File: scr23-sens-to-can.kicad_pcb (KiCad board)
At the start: 2 copper layers, 78 x 62.5 mm, 65 parts, among them IC1 ADS1256IDBRG4, J3 Conn_ST_STDC14, J4 6437288-2, SW1 SW_SPDT, U1 SRV05-4, U2 SRV05-4, U3 LM4040DCK-2.5, U4 TJA1042T-3, U5 AP7370-33Y-13, U6 ADP7142AUJZ-5.0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

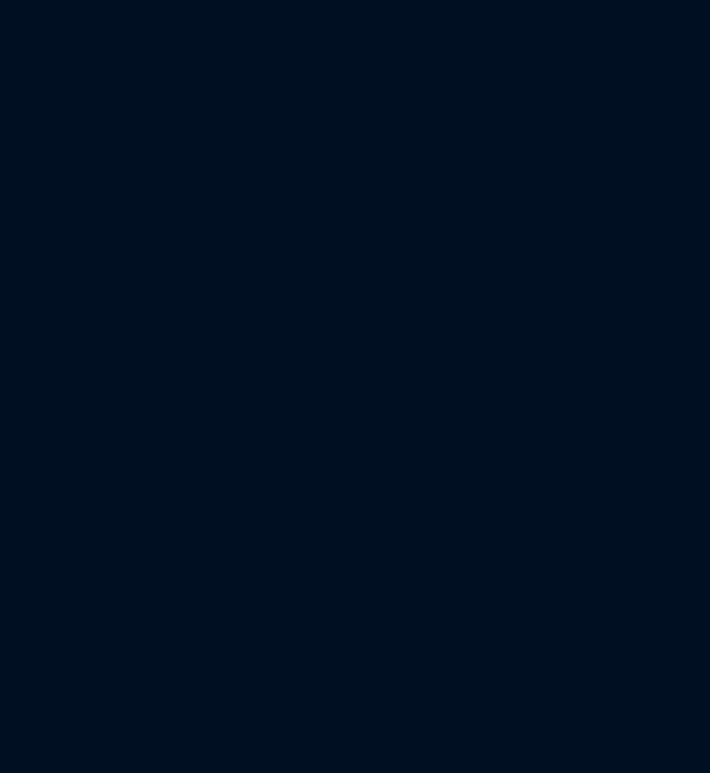
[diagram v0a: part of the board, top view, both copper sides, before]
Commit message: add uC crystal, finish swap to ads8168, need to add some footprints to passives and redo layout
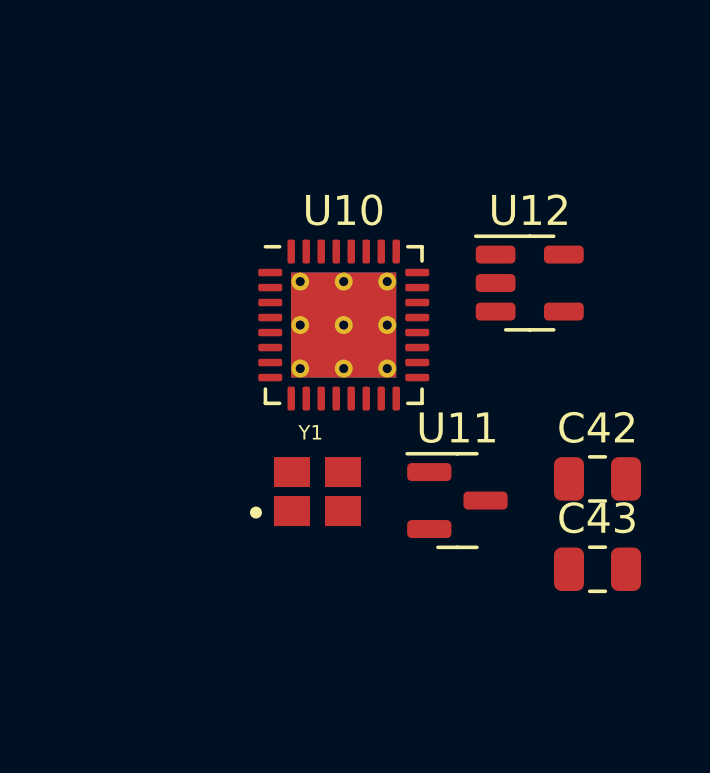
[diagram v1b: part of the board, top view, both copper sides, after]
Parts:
- added C42: 1uF, Capacitor_SMD:C_0805_2012Metric, F.Cu at (178.6, 102.7)
- added C43: 1uF, Capacitor_SMD:C_0805_2012Metric, F.Cu at (178.6, 105.7)
- added U10: ADS8168IRHBT, Package_DFN_QFN:VQFN-32-1EP_5x5mm_P0.5mm_EP3.5x3.5mm_ThermalVias, F.Cu at (170.2, 97.5)
- added U11: LM4040DBZ-5, Package_TO_SOT_SMD:SOT-23, F.Cu at (174.0, 103.4)
- added U12: OPA320AIDBVR, Package_TO_SOT_SMD:SOT-23-5, F.Cu at (176.4, 96.1)
- added Y1: ECS-160-8-36B-CKY-TR3, scr23-sens-to-can-main:XTAL_ECS-163.84-10-36-JGN-TR, F.Cu at (169.3, 103.1)
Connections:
- net /ADC_CS renamed ADC_CS
- U8 pad 11: /DATA_RDY -> DATA_READY
- U8 pad 13: /SPI1_SCK -> ADC_SCLK
- U8 pad 14: /SPI1_MISO -> ADC_SDO
- U8 pad 15: /SPI1_MOSI -> ADC_SDI
- U8 pad 3: Net-(U8A-PC14-OSC32_IN) -> unconnected-(U8A-PC14-OSC32_IN-Pad3)
- U8 pad 4: Net-(U8A-PC15-OSC32_OUT) -> unconnected-(U8A-PC15-OSC32_OUT-Pad4)
- U8 pad 5: Net-(U8A-PF0-OSC_IN) -> /OSC_IN
- U8 pad 6: Net-(U8A-PF1-OSC_OUT) -> /OSC_OUT
